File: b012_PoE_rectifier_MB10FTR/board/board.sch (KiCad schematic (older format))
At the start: 4 parts, among them J1 004_BASE-T_CT_2x3, J2 PoE_2x2

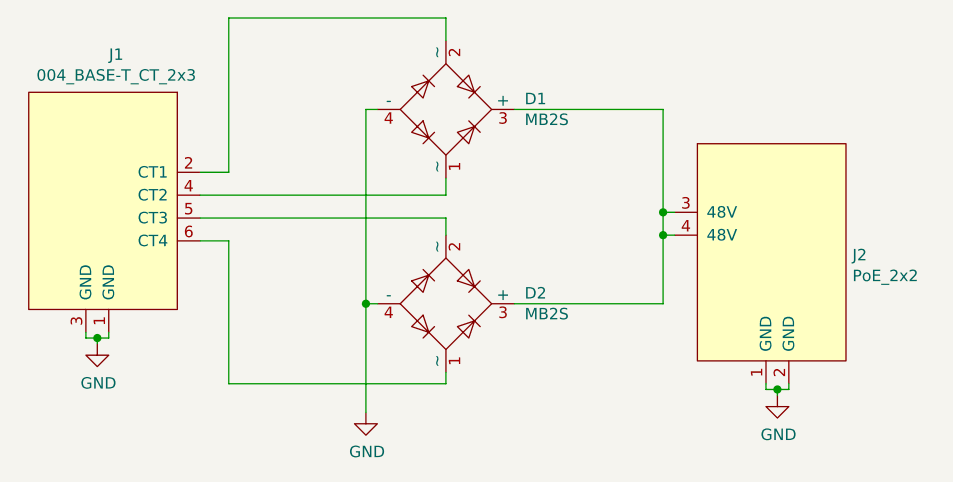
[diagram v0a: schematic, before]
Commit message: added part info for silicon parts
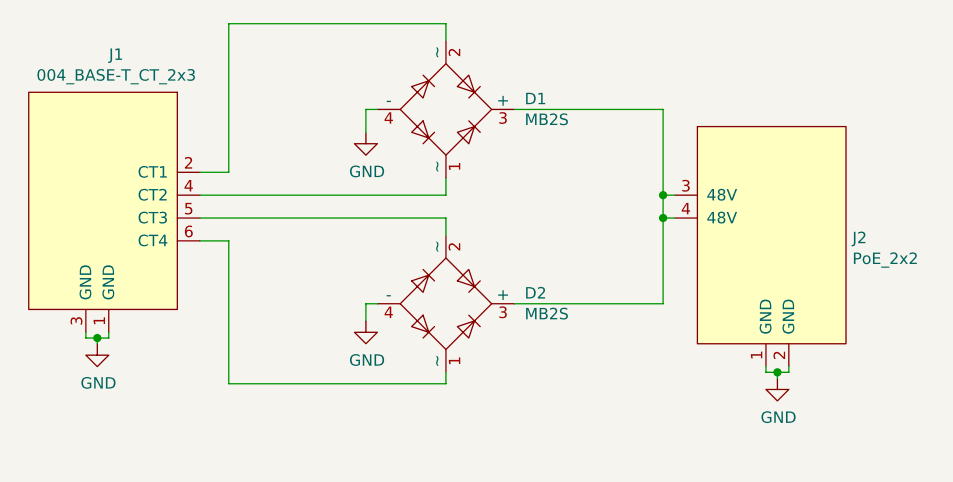
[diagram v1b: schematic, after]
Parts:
- D1, D2: MPN (none) -> MB2S
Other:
- moved on the sheet: J2
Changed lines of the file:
@@
 F 2 "Package_TO_SOT_SMD:TO-269AA" H 5525 3300 50  0001 L CNN
 F 3 "http://www.vishay.com/docs/88661/mb2s.pdf" H 5375 3175 50  0001 C CNN
+F 4 "MB2S" H 5375 3175 50  0001 C CNN "MPN"
 	1    5375 3175
 	1    0    0    -1
@@
 L put_on_edge:PoE_2x2 J2
 U 1 1 6031DED2
-P 6825 3825
-F 0 "J2" H 7153 3838 50  0000 L CNN
-F 1 "PoE_2x2" H 7153 3747 50  0000 L CNN
-F 2 "on_edge:on_edge_2x02_host" H 7125 4475 50  0001 C CNN
-F 3 "" H 7125 4475 50  0001 C CNN
-	1    6825 3825
+P 6825 3750
+F 0 "J2" H 7153 3763 50  0000 L CNN
+F 1 "PoE_2x2" H 7153 3672 50  0000 L CNN
+F 2 "on_edge:on_edge_2x02_host" H 7125 4400 50  0001 C CNN
+F 3 "" H 7125 4400 50  0001 C CNN
+	1    6825 3750
 	1    0    0    -1
 $EndComp
@@
 F 2 "Package_TO_SOT_SMD:TO-269AA" H 5525 4150 50  0001 L CNN
 F 3 "http://www.vishay.com/docs/88661/mb2s.pdf" H 5375 4025 50  0001 C CNN
+F 4 "MB2S" H 5375 4025 50  0001 C CNN "MPN"
 	1    5375 4025
 	1    0    0    -1
 $EndComp
 Wire Wire Line
-	6375 3725 6325 3725
-Wire Wire Line
-	6325 3725 6325 3625
+	6375 3650 6325 3650
 Wire Wire Line
 	6325 3175 5675 3175
 Wire Wire Line
-	6375 3625 6325 3625
-Connection ~ 6325 3625
-Wire Wire Line
-	6325 3625 6325 3175
+	6375 3550 6325 3550
 Wire Wire Line
 	5675 4025 6325 4025
 Wire Wire Line
-	6325 4025 6325 3725
-Connection ~ 6325 3725
-Wire Wire Line
 	5075 4025 5025 4025
 Wire Wire Line
-	5025 4025 5025 4500
+	5025 4025 5025 4100
 $Comp
 L power:GND #PWR0101
 U 1 1 6032009E
-P 5025 4500
-F 0 "#PWR0101" H 5025 4250 50  0001 C CNN
-F 1 "GND" H 5030 4327 50  0000 C CNN
-F 2 "" H 5025 4500 50  0001 C CNN
-F 3 "" H 5025 4500 50  0001 C CNN
-	1    5025 4500
+P 5025 4100
+F 0 "#PWR0101" H 5025 3850 50  0001 C CNN
+F 1 "GND" H 5030 3927 50  0000 C CNN
+F 2 "" H 5025 4100 50  0001 C CNN
+F 3 "" H 5025 4100 50  0001 C CNN
+	1    5025 4100
 	1    0    0    -1
 $EndComp
@@
 L power:GND #PWR0102
 U 1 1 603203AA
-P 6825 4425
-F 0 "#PWR0102" H 6825 4175 50  0001 C CNN
-F 1 "GND" H 6830 4252 50  0000 C CNN
-F 2 "" H 6825 4425 50  0001 C CNN
-F 3 "" H 6825 4425 50  0001 C CNN
-	1    6825 4425
+P 6825 4350
+F 0 "#PWR0102" H 6825 4100 50  0001 C CNN
+F 1 "GND" H 6830 4177 50  0000 C CNN
+F 2 "" H 6825 4350 50  0001 C CNN
+F 3 "" H 6825 4350 50  0001 C CNN
+	1    6825 4350
 	1    0    0    -1
 $EndComp
 Wire Wire Line
-	6775 4375 6775 4400
+	6775 4300 6775 4325
 Wire Wire Line
-	6775 4400 6825 4400
+	6775 4325 6825 4325
 Wire Wire Line
-	6825 4400 6825 4425
+	6825 4325 6825 4350
 Wire Wire Line
-	6825 4400 6875 4400
+	6825 4325 6875 4325
 Wire Wire Line
-	6875 4400 6875 4375
-Connection ~ 6825 4400
-Wire Wire Line
-	5025 4025 5025 3175
+	6875 4325 6875 4300
+Connection ~ 6825 4325
 Wire Wire Line
 	5025 3175 5075 3175
-Connection ~ 5025 4025
 Wire Wire Line
 	4300 3450 4425 3450
 Wire Wire Line
-	4425 3450 4425 2775
+	4425 3450 4425 2800
 Wire Wire Line
-	4425 2775 5375 2775
+	4425 2800 5375 2800
 Wire Wire Line
-	5375 2775 5375 2875
+	5375 2800 5375 2875
 Wire Wire Line
 	4300 3550 5375 3550
@@
 	3900 4175 3900 4150
 Connection ~ 3850 4175
+$Comp
+L power:GND #PWR?
+U 1 1 6043C553
+P 5025 3275
+F 0 "#PWR?" H 5025 3025 50  0001 C CNN
+F 1 "GND" H 5030 3102 50  0000 C CNN
+F 2 "" H 5025 3275 50  0001 C CNN
+F 3 "" H 5025 3275 50  0001 C CNN
+	1    5025 3275
+	1    0    0    -1
+$EndComp
+Wire Wire Line
+	5025 3175 5025 3275
+Connection ~ 6325 3550
+Wire Wire Line
+	6325 3550 6325 3175
+Connection ~ 6325 3650
+Wire Wire Line
+	6325 3650 6325 4025
+Wire Wire Line
+	6325 3550 6325 3650
 $EndSCHEMATC

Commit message: updated connectors
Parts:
- J1: footprint on_edge:on_edge_2x03_device -> on_edge:on_edge_2x05_device; symbol put_on_edge:004_BASE-T_CT_2x3 -> put_on_edge:004_BASE-T_CT
- J2: footprint on_edge:on_edge_2x02_host -> on_edge:on_edge_2x05_host; symbol put_on_edge:PoE_2x2 -> put_on_edge:013_PoE_rectified
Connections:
- net GND: now also J1.10 (GND), J1.5 (GND), J1.7 (GND), J1.9 (GND)
- net at D2.2 (~~): now also J1.6 (CT3); no longer J1.5 (CT3)
- net at D2.1 (~~): now also J1.8 (CT4); no longer J1.6 (CT4)
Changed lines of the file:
@@
 $EndComp
 $Comp
-L put_on_edge:004_BASE-T_CT_2x3 J1
+L put_on_edge:004_BASE-T_CT J1
 U 1 1 6031D679
 P 3850 3600
 F 0 "J1" H 3767 4265 50  0000 C CNN
 F 1 "004_BASE-T_CT_2x3" H 3767 4174 50  0000 C CNN
-F 2 "on_edge:on_edge_2x03_device" H 4150 4250 50  0001 C CNN
+F 2 "on_edge:on_edge_2x05_device" H 4150 4250 50  0001 C CNN
 F 3 "" H 4150 4250 50  0001 C CNN
 	1    3850 3600
@@
 $EndComp
 $Comp
-L put_on_edge:PoE_2x2 J2
+L put_on_edge:013_PoE_rectified J2
 U 1 1 6031DED2
 P 6825 3750
 F 0 "J2" H 7153 3763 50  0000 L CNN
 F 1 "PoE_2x2" H 7153 3672 50  0000 L CNN
-F 2 "on_edge:on_edge_2x02_host" H 7125 4400 50  0001 C CNN
+F 2 "on_edge:on_edge_2x05_host" H 7125 4400 50  0001 C CNN
 F 3 "" H 7125 4400 50  0001 C CNN
 	1    6825 3750
@@
 Wire Wire Line
 	6325 3550 6325 3650
+Wire Wire Line
+	3600 4150 3700 4150
+Connection ~ 3700 4150
+Wire Wire Line
+	3700 4150 3800 4150
+Connection ~ 3800 4150
+Wire Wire Line
+	3800 4150 3900 4150
+Connection ~ 3900 4150
+Wire Wire Line
+	3900 4150 4000 4150
+Connection ~ 4000 4150
+Wire Wire Line
+	4000 4150 4100 4150
 $EndSCHEMATC

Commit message: changed to horizontal style
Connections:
- net GND: now also J2.5 (GND)
- net at D1.1 (~~): now also J1.2 (CT1); no longer J1.4 (CT2)
- net at D1.2 (~~): now also J1.4 (CT2); no longer J1.2 (CT1)
- net at J1.6 (CT3): now also D2.1 (~~); no longer D2.2 (~~)
- net at J1.8 (CT4): now also D2.2 (~~); no longer D2.1 (~~)
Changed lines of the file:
@@
 F 4 "MB2S" H 5375 3175 50  0001 C CNN "MPN"
 	1    5375 3175
-	1    0    0    -1
+	1    0    0    1
 $EndComp
 $Comp
@@
 F 4 "MB2S" H 5375 4025 50  0001 C CNN "MPN"
 	1    5375 4025
-	1    0    0    -1
+	1    0    0    1
 $EndComp
 Wire Wire Line
@@
 Connection ~ 3850 4175
 $Comp
-L power:GND #PWR?
+L power:GND #PWR0104
 U 1 1 6043C553
 P 5025 3275
-F 0 "#PWR?" H 5025 3025 50  0001 C CNN
+F 0 "#PWR0104" H 5025 3025 50  0001 C CNN
 F 1 "GND" H 5030 3102 50  0000 C CNN
 F 2 "" H 5025 3275 50  0001 C CNN
@@
 Wire Wire Line
 	4000 4150 4100 4150
+Wire Wire Line
+	6975 4300 6975 4325
+Wire Wire Line
+	6975 4325 6875 4325
+Connection ~ 6875 4325
 $EndSCHEMATC
